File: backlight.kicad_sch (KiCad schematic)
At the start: 56 parts

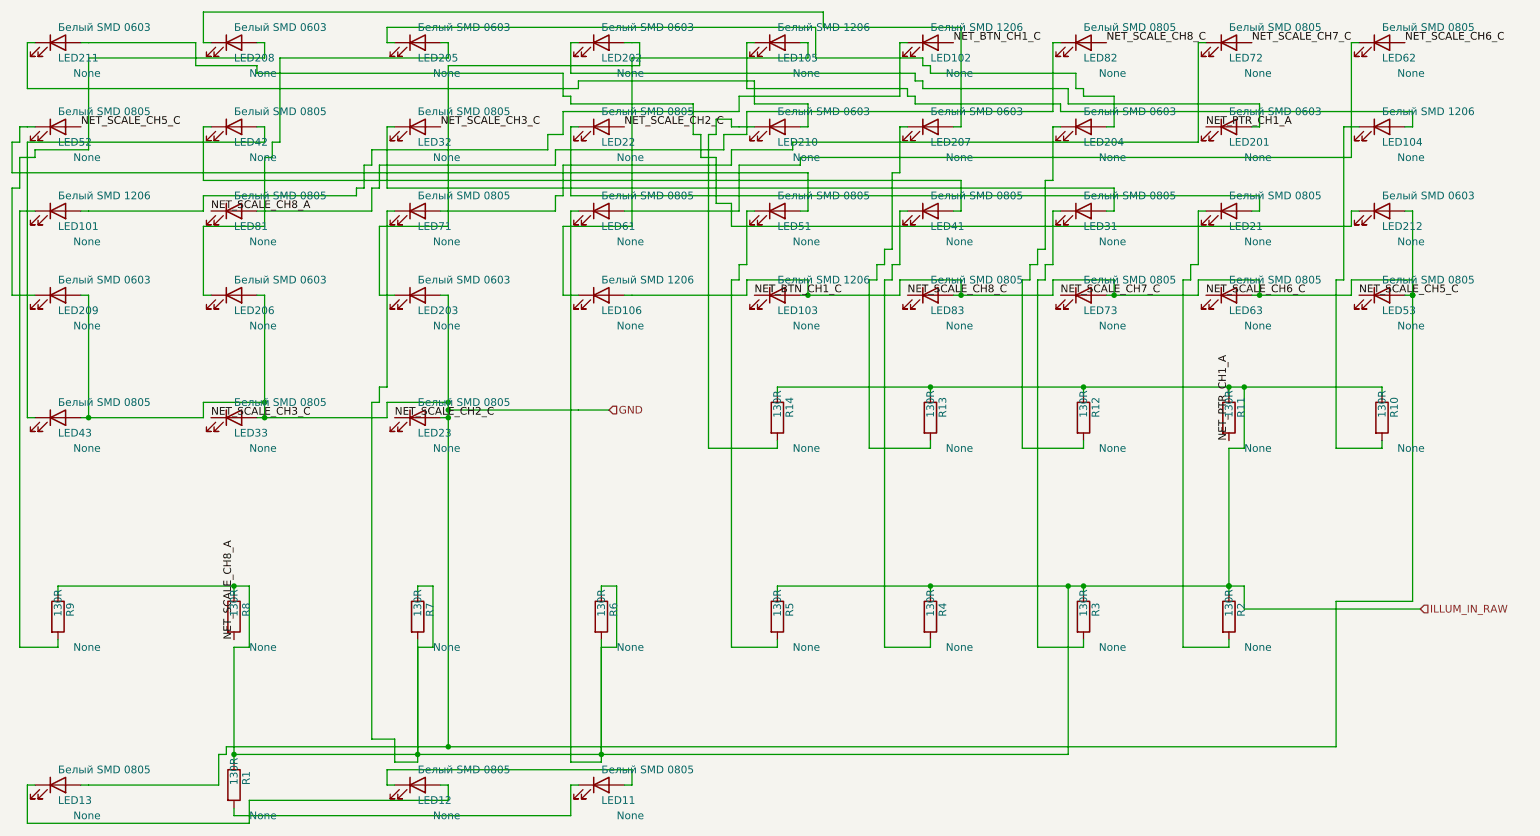
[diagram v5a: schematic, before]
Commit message: реализована 2я занятость клетки
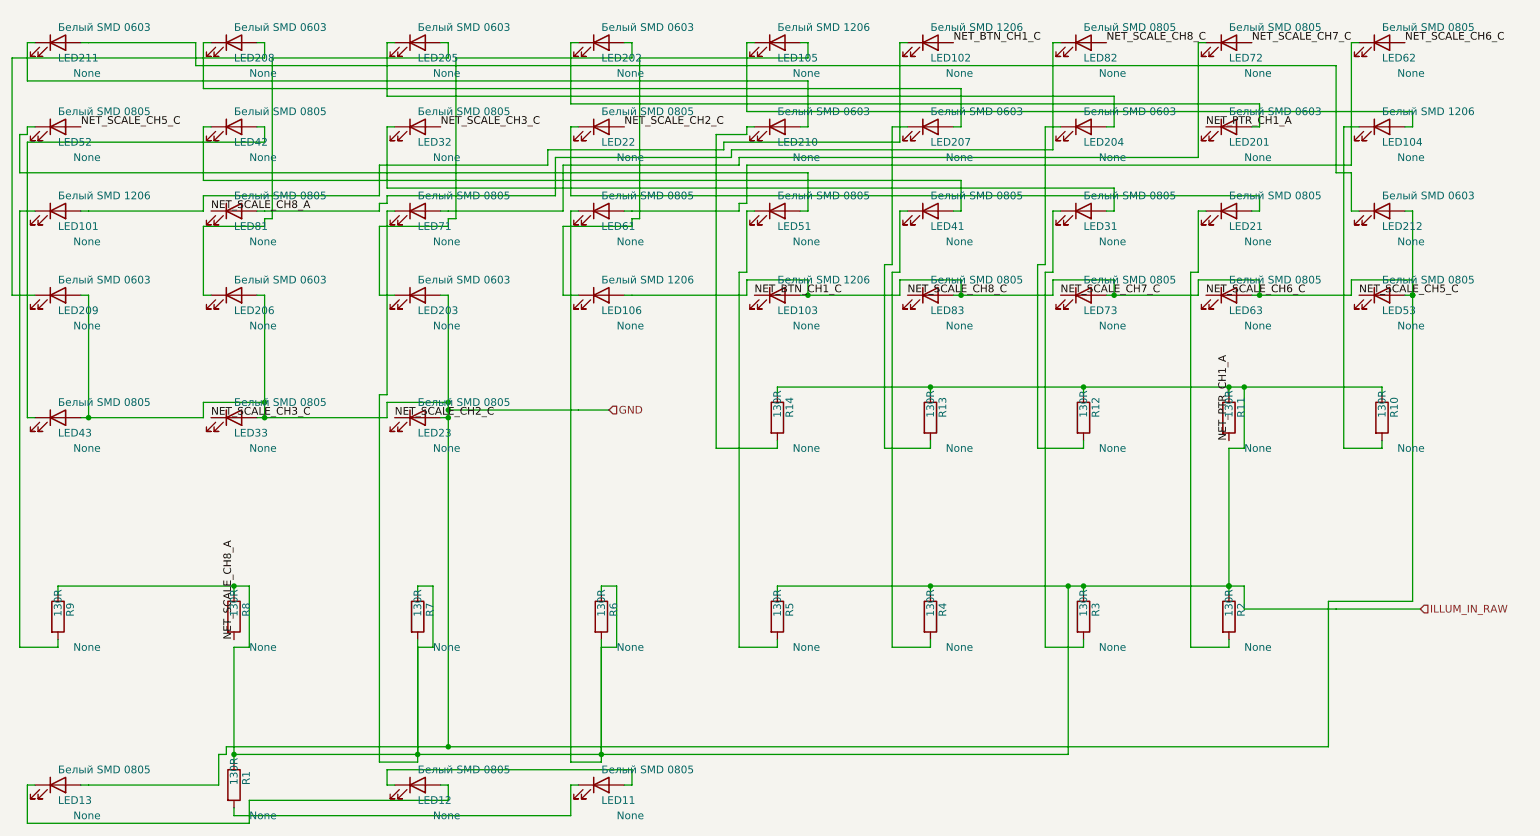
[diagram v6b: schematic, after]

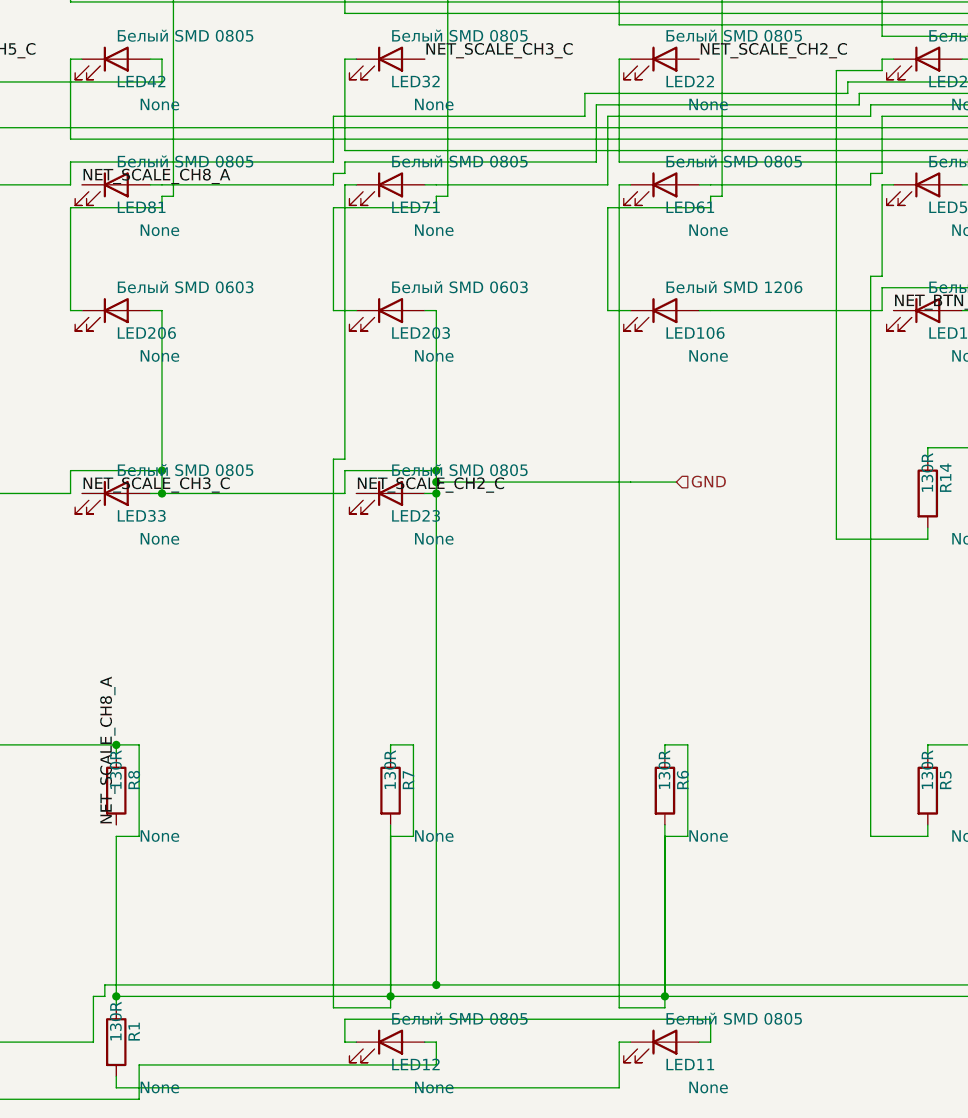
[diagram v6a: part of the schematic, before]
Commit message: фильтр клеток для Т если там пересечение
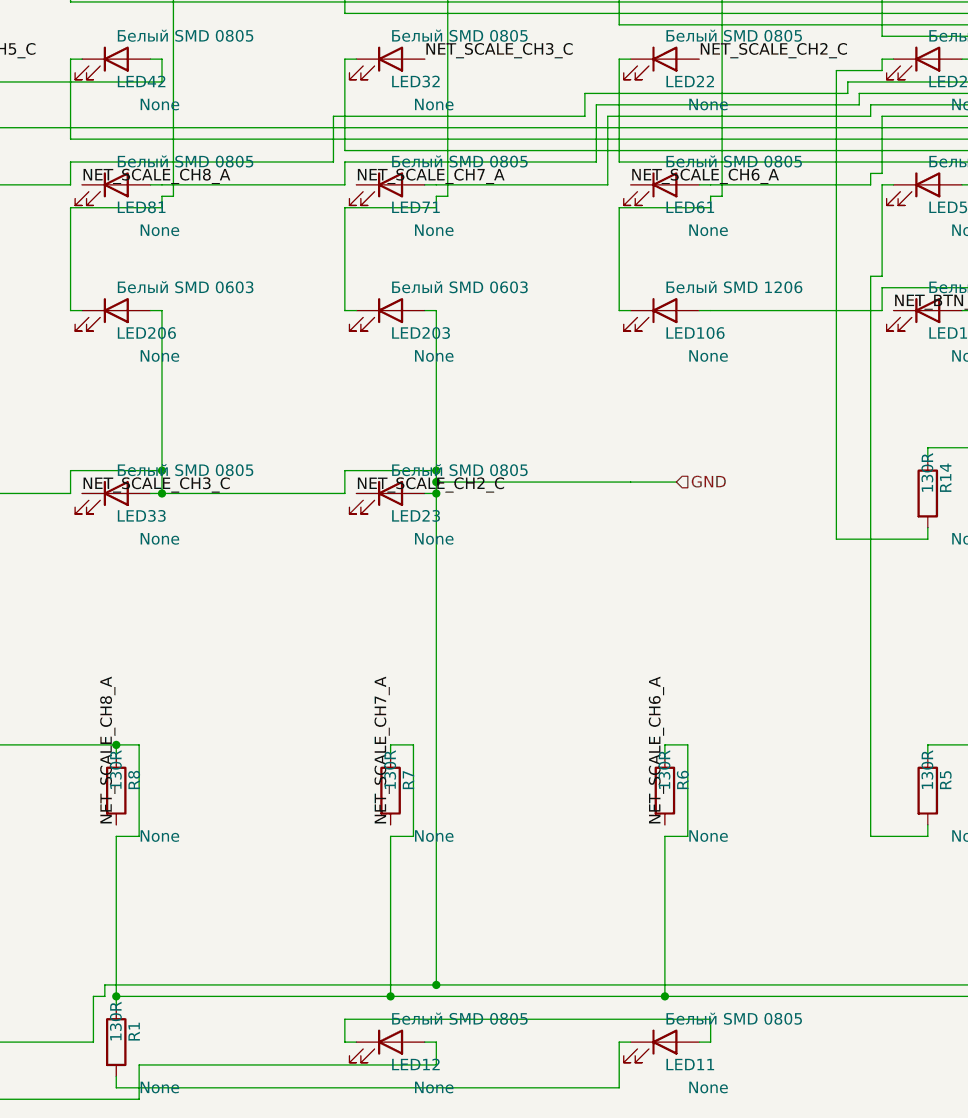
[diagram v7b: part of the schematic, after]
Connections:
- net ILLUM_IN_RAW: no longer LED61.1 (K), LED71.1 (K), R6.2, R7.2
- new net NET_SCALE_CH6_A: LED61.1 (K), R6.2
- new net NET_SCALE_CH7_A: LED71.1 (K), R7.2

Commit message: fic placer for small schemes
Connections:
- net NET_SCALE_CH8_B: now reaches LED81.2 (A), LED82.1 (K)
- net NET_PTR_CH1_B: now reaches LED201.2 (A), LED202.1 (K)
- net NET_SCALE_CH1_A: now reaches LED11.1 (K), R1.2
- net NET_SCALE_CH3_A: now reaches LED31.1 (K), R3.2
- net NET_SCALE_CH1_B: now reaches LED11.2 (A), LED12.1 (K)
- net NET_PTR_CH3_A: now reaches LED207.1 (K), R13.2
- net NET_PTR_CH3_B: now reaches LED207.2 (A), LED208.1 (K)
- net NET_SCALE_CH7_B: now reaches LED71.2 (A), LED72.1 (K)
- net NET_SCALE_CH2_A: now reaches LED21.1 (K), R2.2
- net NET_SCALE_CH3_B: now reaches LED31.2 (A), LED32.1 (K)
- net NET_SCALE_CH1_C: now reaches LED12.2 (A), LED13.1 (K)
- net NET_PTR_CH2_A: now reaches LED204.1 (K), R12.2
- net NET_SCALE_CH6_B: now reaches LED61.2 (A), LED62.1 (K)
- net NET_SCALE_CH5_A: now reaches LED51.1 (K), R5.2
- net NET_BTN_CH1_A: now reaches LED101.1 (K), R9.2
- net NET_PTR_CH1_C: now reaches LED202.2 (A), LED203.1 (K)
- net NET_PTR_CH4_C: now reaches LED211.2 (A), LED212.1 (K)
- net NET_PTR_CH4_B: now reaches LED210.2 (A), LED211.1 (K)
- net NET_BTN_CH2_B: now reaches LED104.2 (A), LED105.1 (K)
- net NET_BTN_CH2_C: now reaches LED105.2 (A), LED106.1 (K)
- net NET_PTR_CH2_B: now reaches LED204.2 (A), LED205.1 (K)
- net NET_PTR_CH2_C: now reaches LED205.2 (A), LED206.1 (K)
- net NET_PTR_CH4_A: now reaches LED210.1 (K), R14.2
- net NET_SCALE_CH4_B: now reaches LED41.2 (A), LED42.1 (K)
- net NET_SCALE_CH4_C: now reaches LED42.2 (A), LED43.1 (K)
- net NET_SCALE_CH4_A: now reaches LED41.1 (K), R4.2
- net NET_SCALE_CH2_B: now reaches LED21.2 (A), LED22.1 (K)
- net NET_BTN_CH2_A: now reaches LED104.1 (K), R10.2
- net NET_BTN_CH1_B: now reaches LED101.2 (A), LED102.1 (K)
- net NET_PTR_CH3_C: now reaches LED208.2 (A), LED209.1 (K)
- net NET_SCALE_CH5_B: now reaches LED51.2 (A), LED52.1 (K)
